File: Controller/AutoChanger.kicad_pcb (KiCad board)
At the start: 2 copper layers, 118 x 32 mm, 48 parts, among them IC1 ATMEGA328P-A, P1 CONNECT, P2 USB_B, P3 1, P4 2, P5 3, P6 4, P7 ICSP, SW1 RESET, SW2 1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

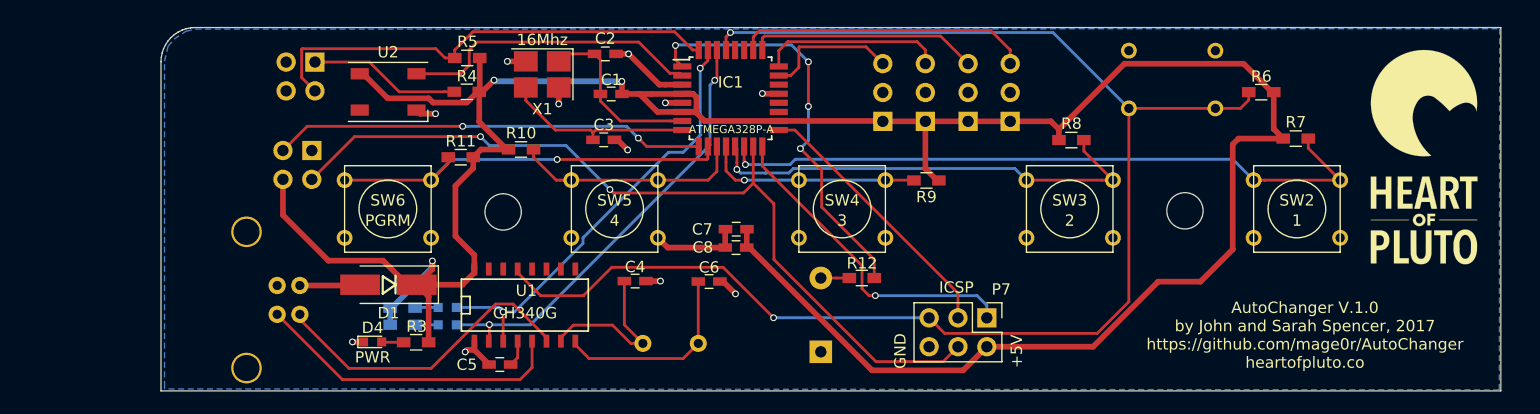
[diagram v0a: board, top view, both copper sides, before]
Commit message: Updated board design.
Heaps more caps.  Thanks @projectgus
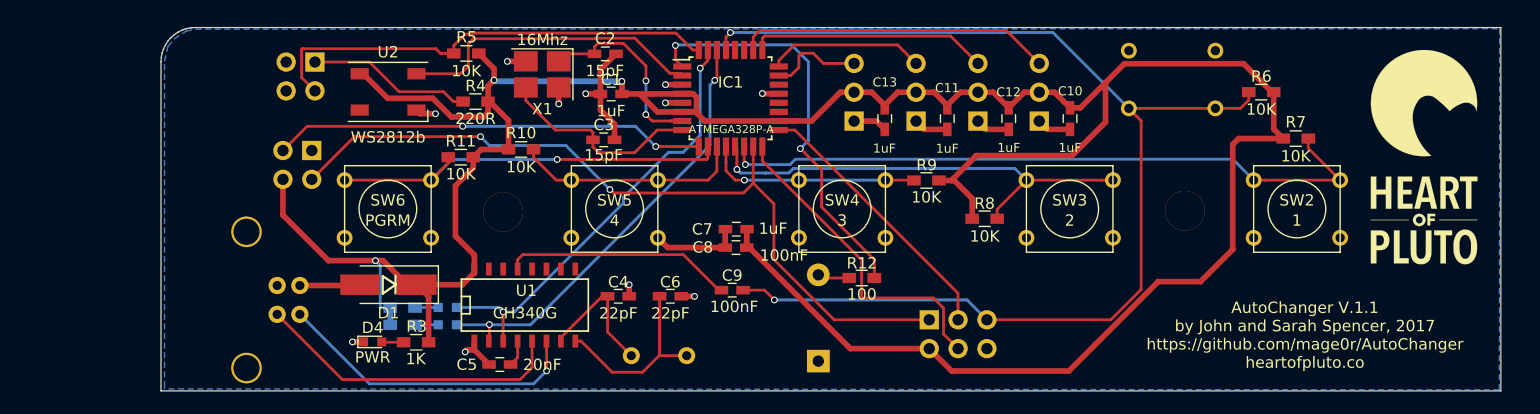
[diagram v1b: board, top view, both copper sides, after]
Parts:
- added C10: 1uF, Capacitors_SMD:C_0603_HandSoldering, F.Cu at (169.2, 88.1)
- added C11: 1uF, Capacitors_SMD:C_0603_HandSoldering, F.Cu at (158.4, 88.1)
- added C12: 1uF, Capacitors_SMD:C_0603_HandSoldering, F.Cu at (163.8, 88.1)
- added C13: 1uF, Capacitors_SMD:C_0603_HandSoldering, F.Cu at (152.9, 88.1)
- added C9: 100nF, Capacitors_SMD:C_0603_HandSoldering, F.Cu at (139.5, 103.2)
- P2: footprint libs:USB_B -> Connect:USB_B
- P7: moved to B.Cu
- SP1: footprint libs:piezo -> Buzzers_Beepers:Buzzer_12x9.5RM7.6
- moved R8 10.3 mm to (161.7, 96.9)
- moved P7 5.07 mm to (156.8, 105.8)
- moved SP1 4.08 mm to (147.1, 109.4)
- moved C6 3.65 mm to (134.1, 103.7)
- moved P3 2.56 mm to (166.5, 88.3)
- moved P6 2.53 mm to (150.2, 88.3)
- moved C4 2.00 mm to (129.5, 103.7)
- moved Y1 1.49 mm to (130.6, 109.0)
- moved R4 1.15 mm to (116.9, 86.6)
- moved P4 0.87 mm to (161.1, 88.3)
- moved P5 0.82 mm to (155.7, 88.3)
- moved R5 0.41 mm to (116.1, 82.3)
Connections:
- C1 pad 1: /XTAL1 -> GND
- P3 pad 1: +5V -> GND
- P3 pad 2: GND -> +5V
- P4 pad 1: +5V -> GND
- P4 pad 2: GND -> +5V
- P5 pad 1: +5V -> GND
- P5 pad 2: GND -> +5V
- P6 pad 1: +5V -> GND
- P6 pad 2: GND -> +5V
- P7 pad 1: /D12 -> /D11
- P7 pad 4: /D11 -> /D12
- U1 pad 13: /RESET -> Net-(C9-Pad2)
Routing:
- net /RESET: track 127.7 -> 105.0 mm
- net Net-(C9-Pad2): track 0.00 -> 20.3 mm
- net +5V: track 236.1 -> 255.7 mm
- net GND: track 31.8 -> 46.2 mm
- net /D11: track 74.0 -> 69.4 mm
- net /A0: track 11.9 -> 8.40 mm
- net Net-(C4-Pad1): track 14.8 -> 12.0 mm
- net /XTAL1: track 15.7 -> 18.3 mm, vias 0 -> 2
- net /A1: track 16.1 -> 13.9 mm
- net /A3: track 25.9 -> 27.8 mm
- net /XTAL2: track 16.8 -> 18.4 mm
- net Net-(R4-Pad2): track 13.5 -> 14.5 mm
- net /A2: track 20.3 -> 21.1 mm
- net /D4: track 26.9 -> 27.5 mm
- net Net-(C6-Pad1): track 17.7 -> 17.1 mm
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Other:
- board text added: "5V"
- board text added: "AutoChanger V.1.1 by John and Sarah Spencer, 2017 https://github.com/mage0r/AutoChanger heartofpluto.co"
- board text removed: "AutoChanger V.1.0 by John and Sarah Spencer, 2017 https://github.com/mage0r/AutoChanger heartofpluto.co"
- board text removed: "ISCP"

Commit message: Updated design
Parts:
- removed C1: 1uF, Capacitors_SMD:C_0603_HandSoldering
- removed the G*** at (200.4, 91.5) (x2)
- removed REF** (x2): M3, Mounting_Holes:MountingHole_3.2mm_M3
- removed X1: 16Mhz, Crystals:Crystal_SMD_3225-4pin_3.2x2.5mm_HandSoldering
- added G***: LOGO, libs:logo, F.Cu at (200.8, 90.1)
- added G***: LOGO, libs:logo, B.Cu at (200.8, 90.1)
- added P10: SENSOR, Pin_Headers:Pin_Header_Straight_1x03_Pitch2.54mm, F.Cu at (100.3, 83.1)
- added P11: SENSOR, Pin_Headers:Pin_Header_Straight_1x03_Pitch2.54mm, F.Cu at (80.4, 86.3)
- added P8: M3, Connect:1pin, F.Cu at (119.3, 96.3)
- added P9: M3, Connect:1pin, F.Cu at (179.4, 96.2)
- added Q1: 2n7002, TO_SOT_Packages_SMD:SOT-23_Handsoldering, F.Cu at (167.9, 104.2)
- added R13: 1M, Resistors_SMD:R_0603_HandSoldering, F.Cu at (123.2, 87.2)
- added Y2: 16Mhz, Crystals:Crystal_HC49-U_Vertical, B.Cu at (125.7, 84.5)
- added _: _, Pin_Headers:Pin_Header_Straight_1x04_Pitch1.27mm, F.Cu at (88.1, 92.8)
- C2, C3: value 15pF -> 22pF
- R4, R5: moved to B.Cu
- U3: footprint Pin_Headers:Pin_Header_Angled_2x02_Pitch2.54mm -> libs:ITR9606; moved to F.Cu
- moved R4 38.0 mm to (79.8, 94.8), turned to 270 degrees
- moved R5 34.1 mm to (84.3, 94.8), turned to 90 degrees
- moved U3 23.8 mm to (82.1, 94.8), turned to 90 degrees
- moved C9 0.74 mm to (139.0, 103.7)
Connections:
- C10 pad 2: +5V -> /PWR_DOWN
- C11 pad 2: +5V -> /PWR_DOWN
- C12 pad 2: +5V -> /PWR_DOWN
- C13 pad 2: +5V -> /PWR_DOWN
- P3 pad 2: +5V -> /PWR_DOWN
- P4 pad 2: +5V -> /PWR_DOWN
- P5 pad 2: +5V -> /PWR_DOWN
- P6 pad 2: +5V -> /PWR_DOWN
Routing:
- net /PWR_DOWN: track 0.00 -> 47.8 mm
- net Net-(R4-Pad2): track 14.5 -> 5.07 mm
- net /D2: track 41.1 -> 50.2 mm
- net /D13: track 23.9 -> 32.4 mm
- net +5V: track 255.7 -> 250.3 mm, vias 3 -> 5
- net /XTAL1: track 18.3 -> 21.4 mm
- net /RESET: track 105.0 -> 107.0 mm
- net GND: track 46.2 -> 44.3 mm, vias 11 -> 9
- net /XTAL2: track 18.4 -> 19.9 mm
- added copper zone on F.Cu, net GND
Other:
- board size 118 x 32 mm -> 130.1 x 32 mm
- board text added: "D2"
- board text added: "SENSOR"
- board text removed: "D3"

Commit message: Updated circuit board
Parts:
- removed G*** (x2): LOGO, libs:logo
- removed Q1: 2n7002, TO_SOT_Packages_SMD:SOT-23_Handsoldering
- removed _: _, Pin_Headers:Pin_Header_Straight_1x04_Pitch1.27mm
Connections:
- C10 pad 2: /PWR_DOWN -> +5V
- C11 pad 2: /PWR_DOWN -> +5V
- C12 pad 2: /PWR_DOWN -> +5V
- C13 pad 2: /PWR_DOWN -> +5V
- P3 pad 2: /PWR_DOWN -> +5V
- P4 pad 2: /PWR_DOWN -> +5V
- P5 pad 2: /PWR_DOWN -> +5V
- P6 pad 2: /PWR_DOWN -> +5V
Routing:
- net /PWR_DOWN: track 47.8 -> 0.00 mm
- net +5V: track 250.3 -> 274.8 mm, vias 5 -> 3
- net /D13: track 32.4 -> 23.9 mm
- net GND: track 44.3 -> 51.9 mm
- net /RESET: track 107.0 -> 101.9 mm, vias 2 -> 3
- net /D+: track 27.6 -> 25.9 mm, vias 0 -> 1
- net /D-: track 28.1 -> 28.2 mm, vias 1 -> 0

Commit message: Updated version
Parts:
- added P12: LOGO, libs:logo, B.Cu at (201.1, 90.5)
- added P12: LOGO, libs:logo, F.Cu at (201.1, 90.5)
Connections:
- P7 pad 1: /D11 -> /D12
- P7 pad 4: /D12 -> /D11
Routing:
- net /D12: track 28.6 -> 24.2 mm
- net /D11: track 69.4 -> 73.0 mm

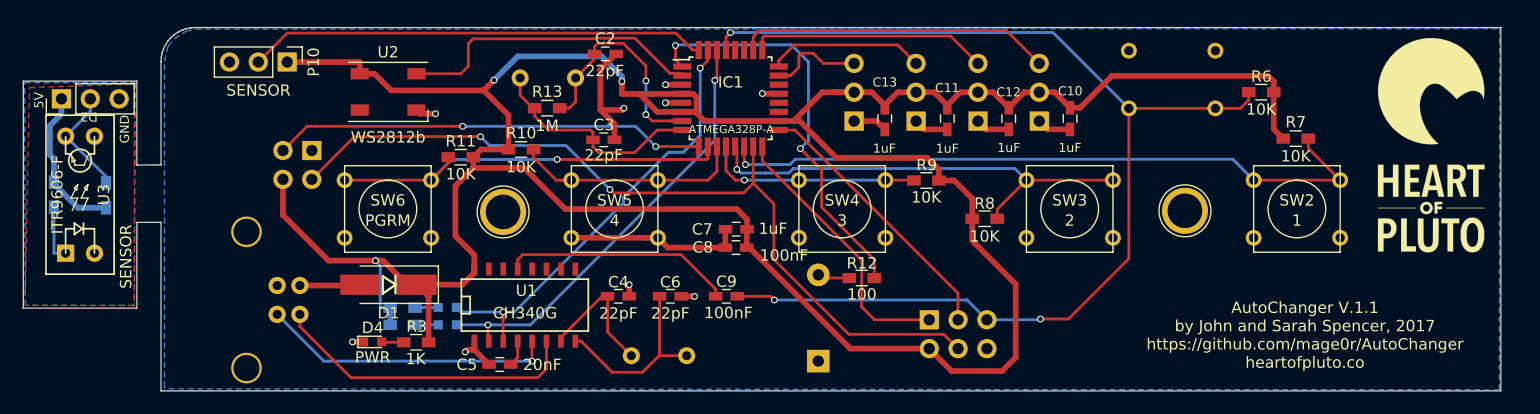
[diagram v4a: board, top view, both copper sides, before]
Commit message: New Nano version
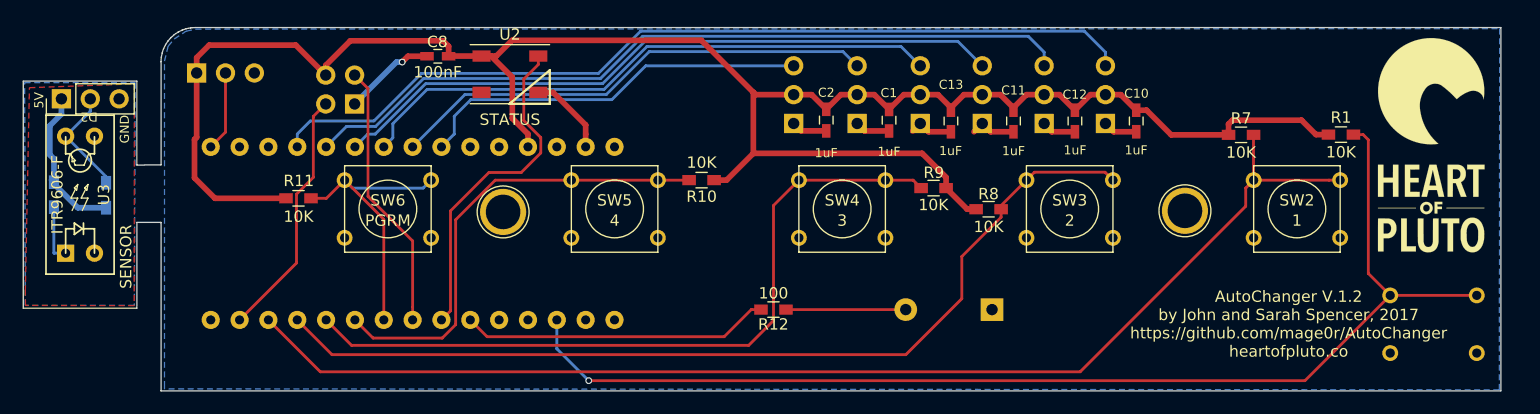
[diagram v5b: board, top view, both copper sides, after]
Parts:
- removed C3, C4, C6: 22pF, Capacitors_SMD:C_0603_HandSoldering
- removed C5: 20nF, Capacitors_SMD:C_0603_HandSoldering
- removed C7: 1uF, Capacitors_SMD:C_0603_HandSoldering
- removed C9: 100nF, Capacitors_SMD:C_0603_HandSoldering
- removed D1: D, Diodes_SMD:D_SMA_Handsoldering
- removed D2: RX, LEDs:LED_0603
- removed D3: TX, LEDs:LED_0603
- removed D4: PWR, LEDs:LED_0603
- removed IC1: ATMEGA328P-A, Housings_QFP:TQFP-32_7x7mm_Pitch0.8mm
- removed P2: USB_B, Connect:USB_B
- removed R13: 1M, Resistors_SMD:R_0603_HandSoldering
- removed R2, R3: 1K, Resistors_SMD:R_0603_HandSoldering
- removed R6: 10K, Resistors_SMD:R_0603_HandSoldering
- removed Y1: 12Mhz, Crystals:Crystal_HC49-U_Vertical
- removed Y2: 16Mhz, Crystals:Crystal_HC49-U_Vertical
- added C1: 1uF, Capacitors_SMD:C_0603_HandSoldering, F.Cu at (153.3, 88.2)
- added P13: 5, Pin_Headers:Pin_Header_Straight_1x03_Pitch2.54mm, B.Cu at (150.5, 88.5)
- C2: value 22pF -> 1uF
- P1: footprint Pin_Headers:Pin_Header_Angled_2x02_Pitch2.54mm -> Pin_Headers:Pin_Header_Straight_2x02_Pitch2.54mm
- P10: moved to B.Cu
- P7: value ICSP -> 6; footprint Pin_Headers:Pin_Header_Straight_2x03_Pitch2.54mm -> Pin_Headers:Pin_Header_Straight_1x03_Pitch2.54mm
- R1: value 1K -> 10K; moved to F.Cu
- U1: value CH340G -> arduino_nano; footprint SMD_Packages:SO-16-N -> arduino:nano; moved to B.Cu
- U2: value WS2812b -> STATUS
- moved R1 84.0 mm to (193.1, 89.5)
- moved SW1 31.5 mm to (201.3, 106.2), turned to 180 degrees
- moved C8 31.2 mm to (113.6, 82.6)
- moved P7 21.0 mm to (144.9, 88.5), turned to 0 degrees
- moved C2 20.3 mm to (147.8, 88.2), turned to 90 degrees
- moved R10 16.1 mm to (136.8, 93.5), turned to 180 degrees
- moved SP1 16.0 mm to (162.4, 104.9), turned to 180 degrees
- moved R11 14.7 mm to (101.3, 95.1), turned to 0 degrees
- moved U1 11.7 mm to (111.3, 98.2), turned to 270 degrees
- moved U2 10.8 mm to (119.9, 84.2)
- moved R12 8.26 mm to (143.1, 104.9), turned to 0 degrees
- moved P10 8.03 mm to (92.3, 84.0)
- moved C10 5.83 mm to (175.1, 88.3)
- moved C11 5.83 mm to (164.3, 88.3)
- moved C12 5.83 mm to (169.7, 88.3)
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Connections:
- net Net-(U1-Pad10) renamed /A6
- net Net-(U1-Pad11) renamed /A7
- net Net-(U1-Pad15) renamed /VIN
- C2 pad 2: /XTAL1 -> +5V
- P10 pad 2: /D2 -> /D13
- P11 pad 2: /D2 -> /D13
- P3 pad 3: /A3 -> /A0
- P4 pad 3: /A2 -> /A1
- P5 pad 3: /A1 -> /A2
- P6 pad 3: /A0 -> /A3
- P7 pad 1: /D12 -> GND
- P7 pad 3: /D13 -> /A5
- R1 pad 2: Net-(D2-Pad2) -> /RESET
- R5 pad 2: /D2 -> /D13
- U1 pad 1: GND -> /D13
- U1 pad 12: Net-(U1-Pad12) -> +5V
- U1 pad 13: Net-(C9-Pad2) -> /RESET
- U1 pad 14: Net-(U1-Pad14) -> GND
- U1 pad 16: +5V -> /TXD
- U1 pad 2: /TXD -> /3V3
- U1 pad 3: /RXD -> /AREF
- U1 pad 4: Net-(C5-Pad1) -> /A0
- U1 pad 5: /D+ -> /A1
- U1 pad 6: /D- -> /A2
- U1 pad 7: Net-(C4-Pad1) -> /A3
- U1 pad 8: Net-(C6-Pad1) -> /A4
- U1 pad 9: Net-(U1-Pad9) -> /A5
- U3 pad 3: /D2 -> /D13
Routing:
- net +5V: track 274.8 -> 192.0 mm, vias 3 -> 0
- net /A0: track 8.40 -> 78.0 mm
- net /A1: track 13.9 -> 69.1 mm
- net /D11: track 73.0 -> 22.2 mm, vias 2 -> 0
- net /D2: track 50.2 -> 0.00 mm
- net /D10: track 59.8 -> 108.2 mm, vias 1 -> 0
- net /D8: track 19.5 -> 66.0 mm, vias 1 -> 0
- net /A4: track 0.00 -> 43.1 mm
- net /D9: track 40.4 -> 82.8 mm, vias 1 -> 0
- net /TXD: track 39.1 -> 0.00 mm, vias 2 -> 0
- net /A2: track 21.1 -> 60.0 mm
- net /RXD: track 38.7 -> 0.00 mm, vias 2 -> 0
- net /A5: track 0.00 -> 34.9 mm
- net /D-: track 28.2 -> 0.00 mm
- net /D+: track 25.9 -> 0.00 mm, vias 1 -> 0
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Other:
- board text added: "AutoChanger V.1.2 by John and Sarah Spencer, 2017 https://github.com/mage0r/AutoChanger heartofpluto.co"
- board text added: "RX D11"
- board text added: "TX D5"
- board text removed: "AutoChanger V.1.1 by John and Sarah Spencer, 2017 https://github.com/mage0r/AutoChanger heartofpluto.co"
- board text removed: "RX"
- board text removed: "TX"
